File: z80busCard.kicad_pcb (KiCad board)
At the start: 2 copper layers, 115.6 x 78.7 mm, 14 parts, among them J1 Conn_02x20_Odd_Even, J2 Conn_02x20_Odd_Even, J3 Conn_02x20_Odd_Even, J4 Conn_02x20_Odd_Even, J5 USB_C_Receptacle_PowerOnly_6P, SW1 SW_Push

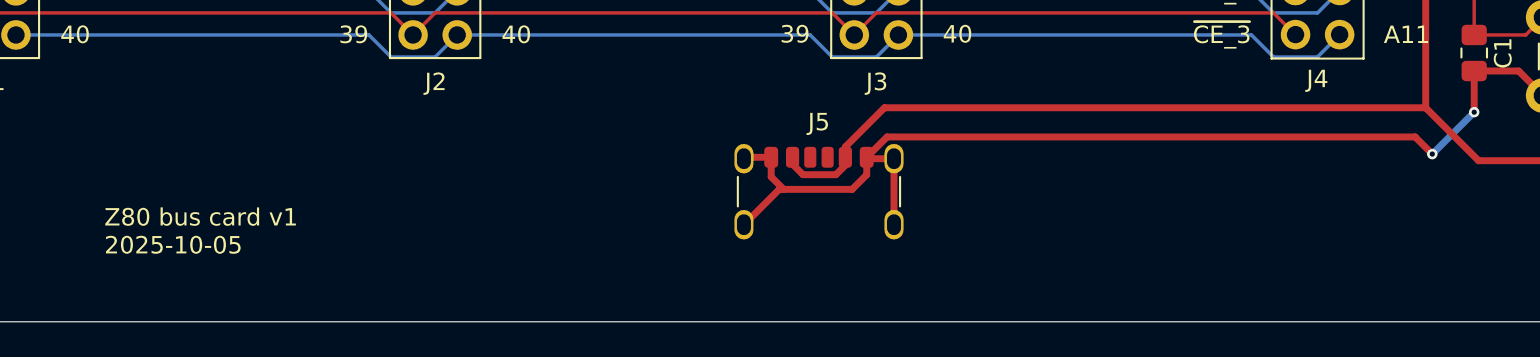
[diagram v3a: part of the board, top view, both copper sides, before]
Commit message: Fixed USB-C power with pull-downs.  Moved connector to the side
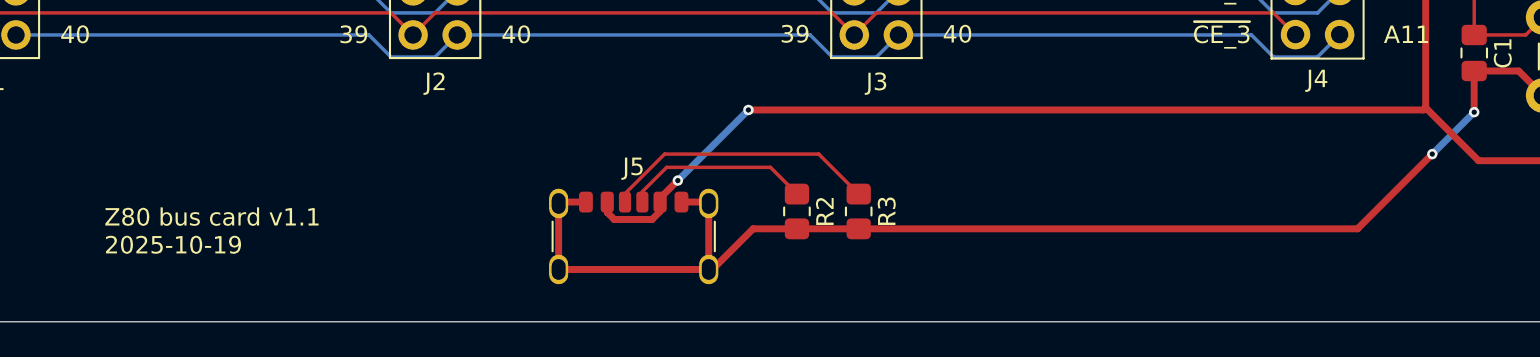
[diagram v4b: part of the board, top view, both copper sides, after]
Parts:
- added R2: 5.1k, Resistor_SMD:R_0805_2012Metric_Pad1.20x1.40mm_HandSolder, F.Cu at (98.3, 134.6)
- added R3: 5.1k, Resistor_SMD:R_0805_2012Metric_Pad1.20x1.40mm_HandSolder, F.Cu at (101.9, 134.6)
- moved J5 11.0 mm to (88.9, 137.2)
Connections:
- J5 pad A5: unconnected-(J5-CC1-PadA5) -> Net-(J5-CC1)
- J5 pad B5: unconnected-(J5-CC2-PadB5) -> Net-(J5-CC2)
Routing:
- net Net-(J5-CC1): track 0.00 -> 15.8 mm
- net GND: track 245.9 -> 257.9 mm
- net +5V: track 196.2 -> 207.9 mm, vias 0 -> 2
- net Net-(J5-CC2): track 0.00 -> 10.7 mm
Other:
- board text added: "Z80 bus card v1.1 2025-10-19"
- board text removed: "Z80 bus card v1 2025-10-05"

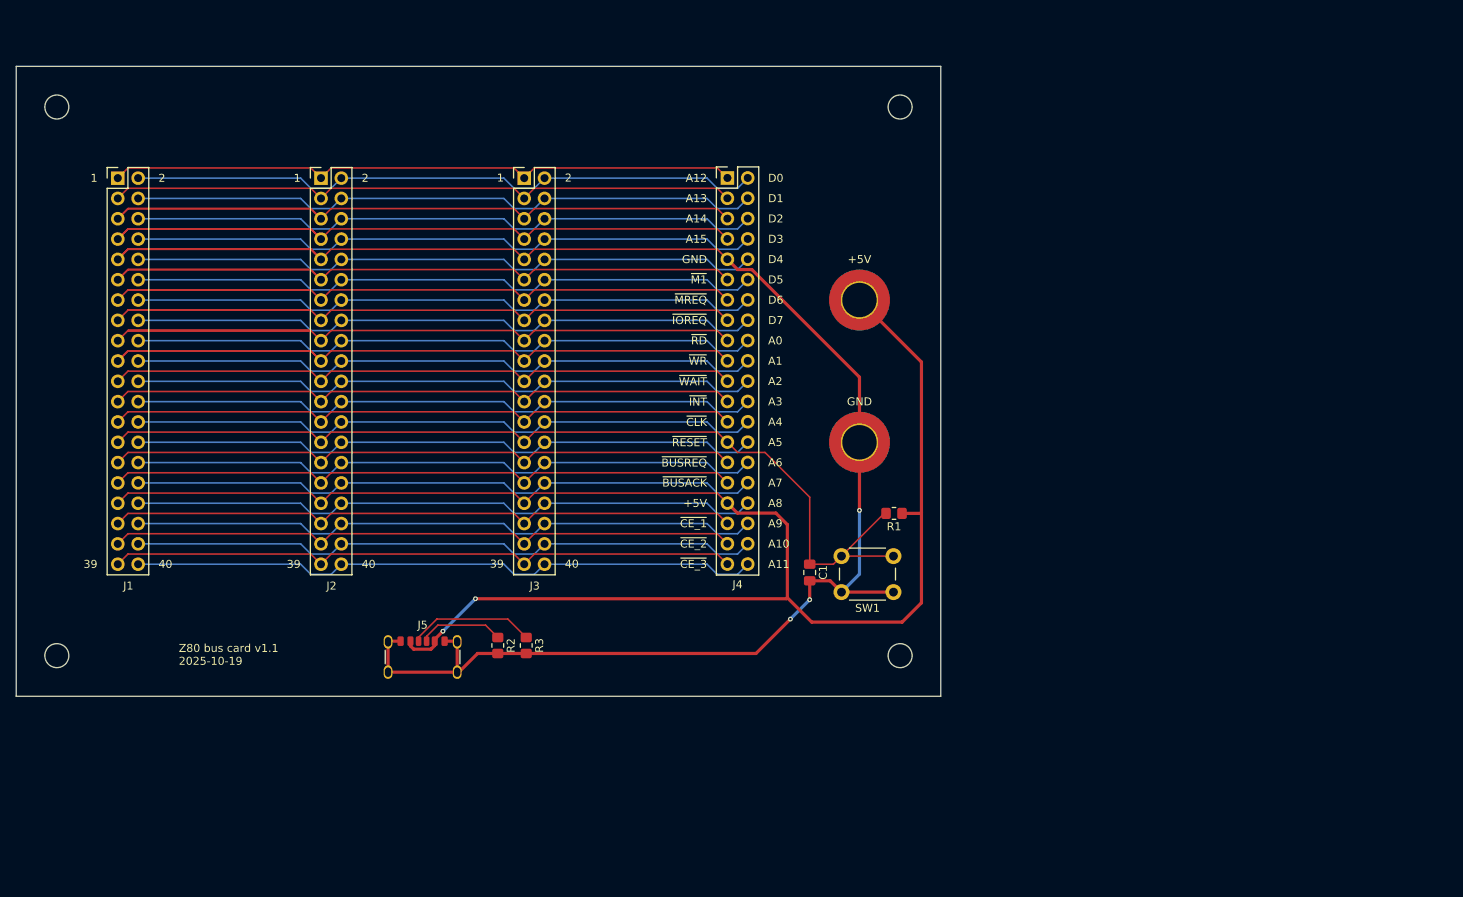
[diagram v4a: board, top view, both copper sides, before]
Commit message: Added power diode
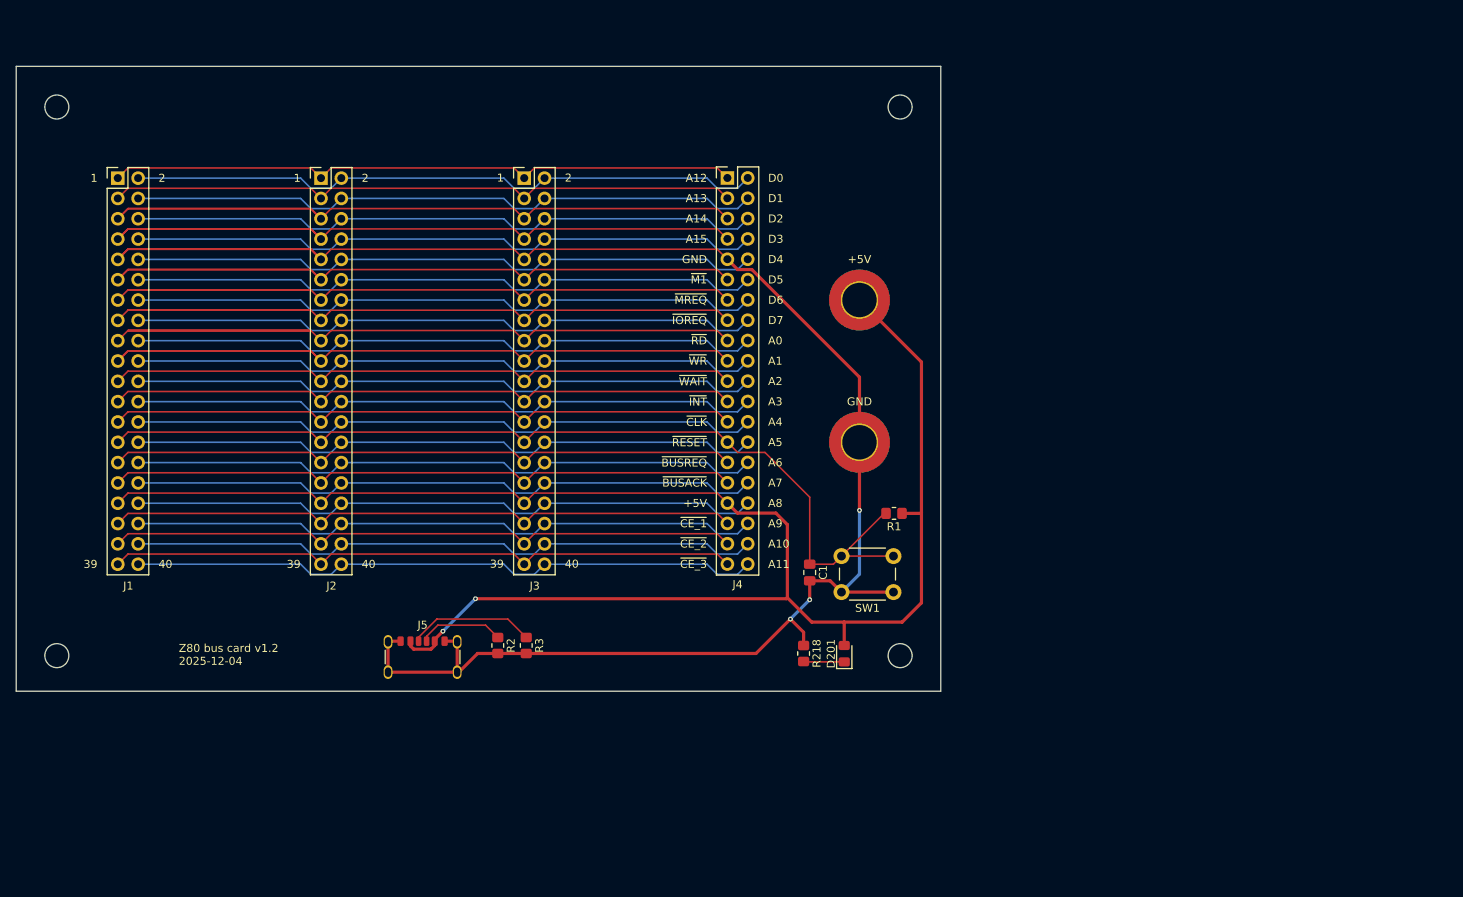
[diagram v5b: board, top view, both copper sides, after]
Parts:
- added D201: LED, LED_SMD:LED_0805_2012Metric_Pad1.15x1.40mm_HandSolder, F.Cu at (141.6, 135.6)
- added R218: 470, Resistor_SMD:R_0805_2012Metric_Pad1.20x1.40mm_HandSolder, F.Cu at (136.5, 135.6)
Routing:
- net Net-(D201-K): track 0.00 -> 5.10 mm
- net GND: track 257.9 -> 261.9 mm
- net +5V: track 207.9 -> 210.8 mm
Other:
- board size 115.6 x 78.7 mm -> 115.6 x 78.1 mm
- board text added: "Z80 bus card v1.2 2025-12-04"
- board text removed: "Z80 bus card v1.1 2025-10-19"

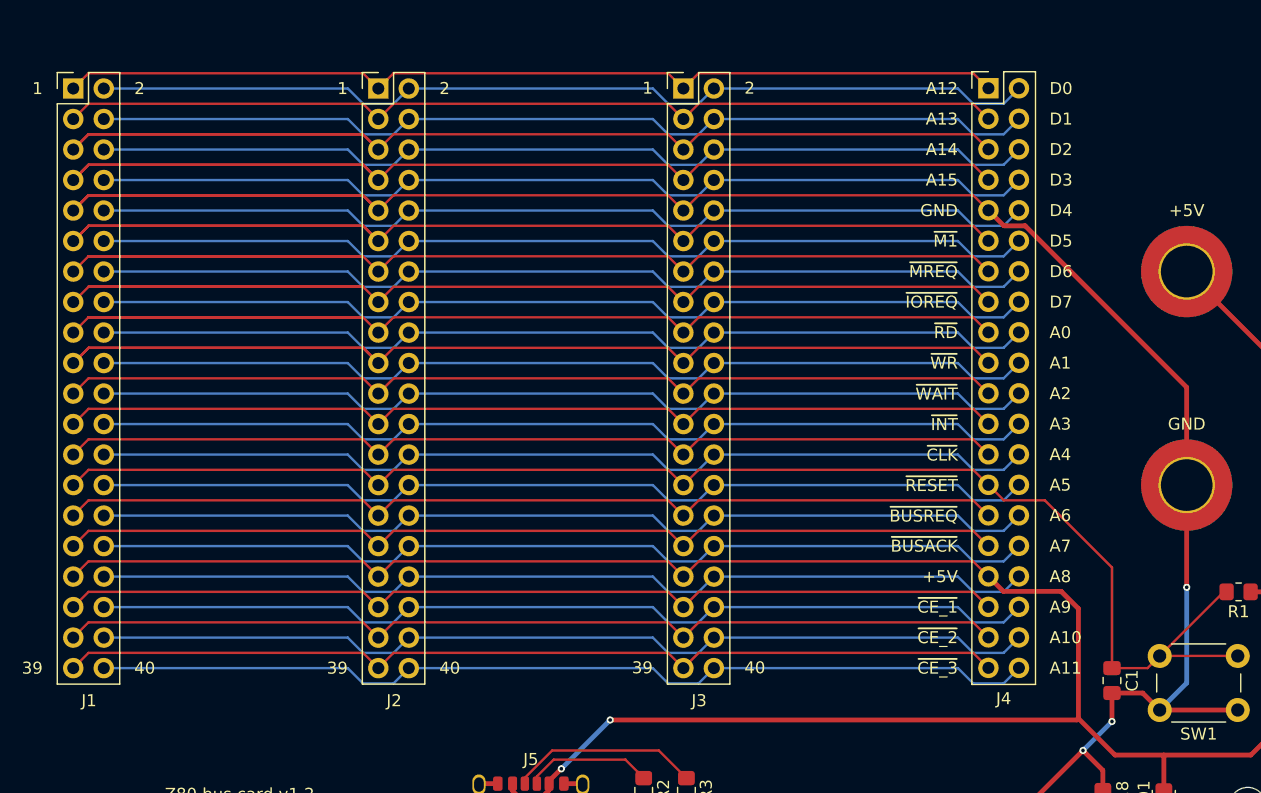
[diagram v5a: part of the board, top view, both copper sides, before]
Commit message: Upgraded to kicad 10, preparing for ground plane
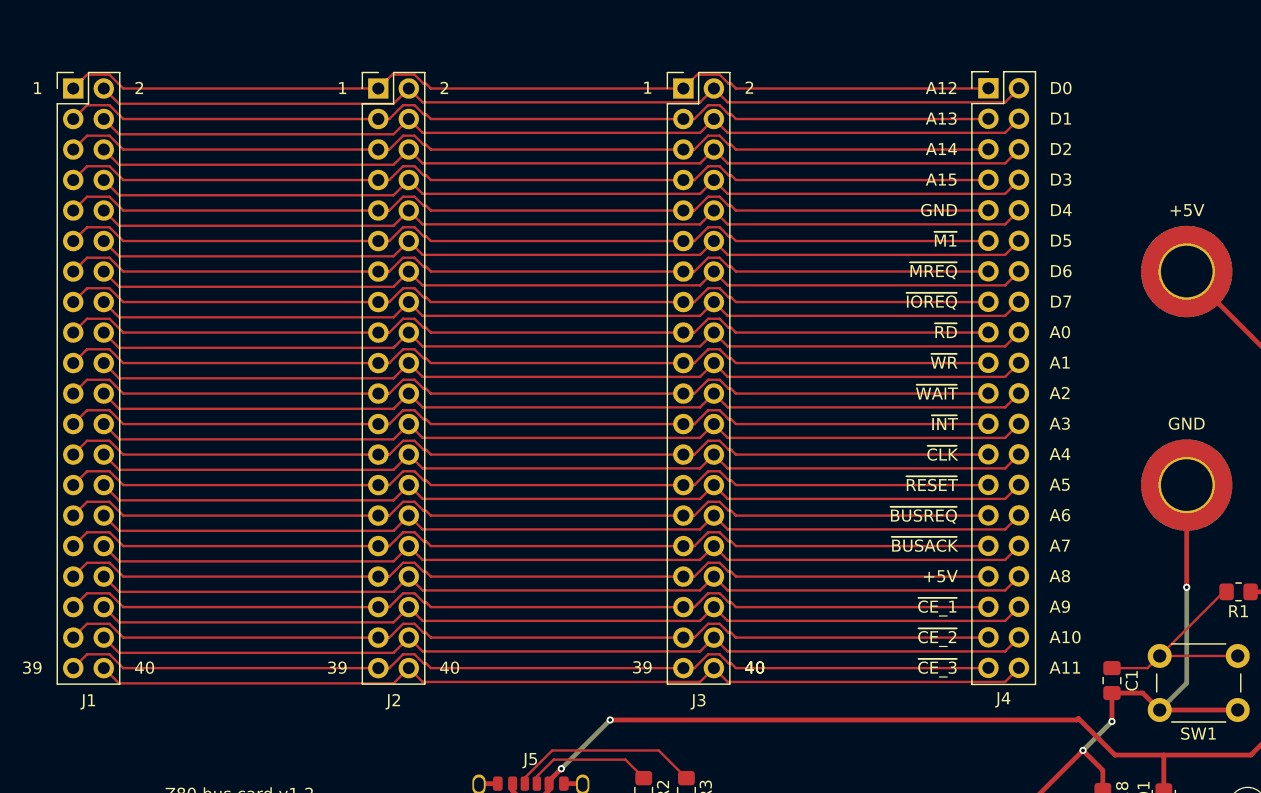
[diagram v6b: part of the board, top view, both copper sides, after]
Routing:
- net GND: track 261.9 -> 180.6 mm
- net /~{RD}: track 125.1 -> 79.1 mm
- net /~{MREQ}: track 125.1 -> 79.1 mm
- net /~{IOREQ}: track 125.1 -> 79.1 mm
- net /~{M1}: track 105.8 -> 79.1 mm
- net /A15: track 105.8 -> 79.1 mm
- net /A14: track 105.8 -> 79.1 mm
- net /~{WR}: track 105.8 -> 79.1 mm
- net /~{RESET}: track 119.5 -> 97.7 mm
- net +5V: track 210.8 -> 192.8 mm

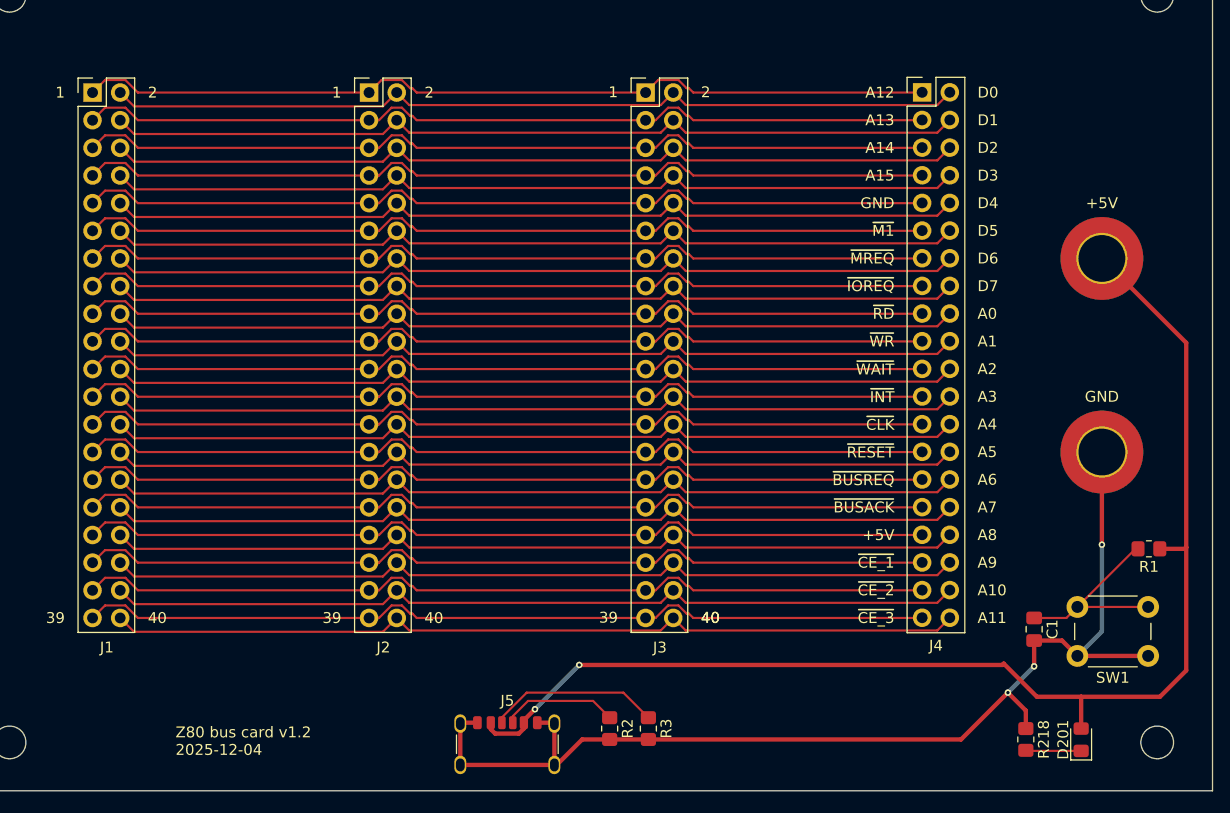
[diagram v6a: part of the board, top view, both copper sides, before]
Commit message: GND and +5V planes
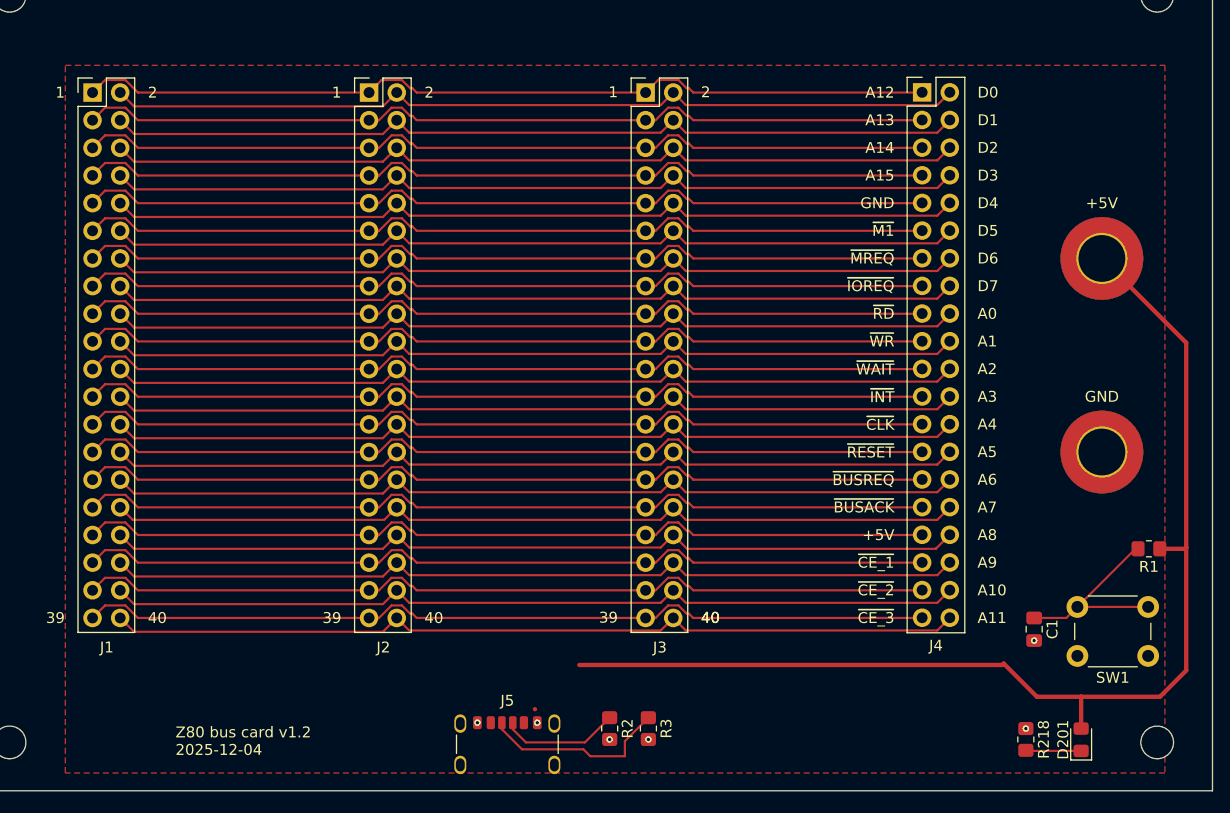
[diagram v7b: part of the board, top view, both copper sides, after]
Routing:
- net GND: track 180.6 -> 79.1 mm, vias 3 -> 6
- net +5V: track 192.8 -> 181.1 mm, vias 2 -> 0
- net Net-(J5-CC1): track 15.8 -> 17.4 mm
- added copper zone on F.Cu, net +5V

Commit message: Replaced Mounting Hole with Mounting hole pad
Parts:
- removed +5V, GND: MountingHole_4.3mm_M4_ISO7380_Pad_TopBottom, MountingHole:MountingHole_4.3mm_M4_ISO7380_Pad_TopBottom
- added H1: MountingHole_Pad, MountingHole:MountingHole_4.3mm_M4_ISO14580_Pad_TopBottom, F.Cu at (143.8, 91.7)
- added H2: MountingHole_Pad, MountingHole:MountingHole_4.3mm_M4_ISO14580_Pad_TopBottom, F.Cu at (143.8, 109.2)
- moved R1 11.1 mm to (137.2, 121.3), turned to -90 degrees
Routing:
- net +5V: track 181.1 -> 79.3 mm
- net /~{RESET}: track 97.7 -> 113.2 mm
- added copper zone on B.Cu, net GND
